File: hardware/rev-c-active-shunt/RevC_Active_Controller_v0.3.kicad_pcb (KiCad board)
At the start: 2 copper layers, 60 x 40 mm, 29 parts, among them J1 TEST_A / GND, J2 +12 GND -12, U1 OPA551PA

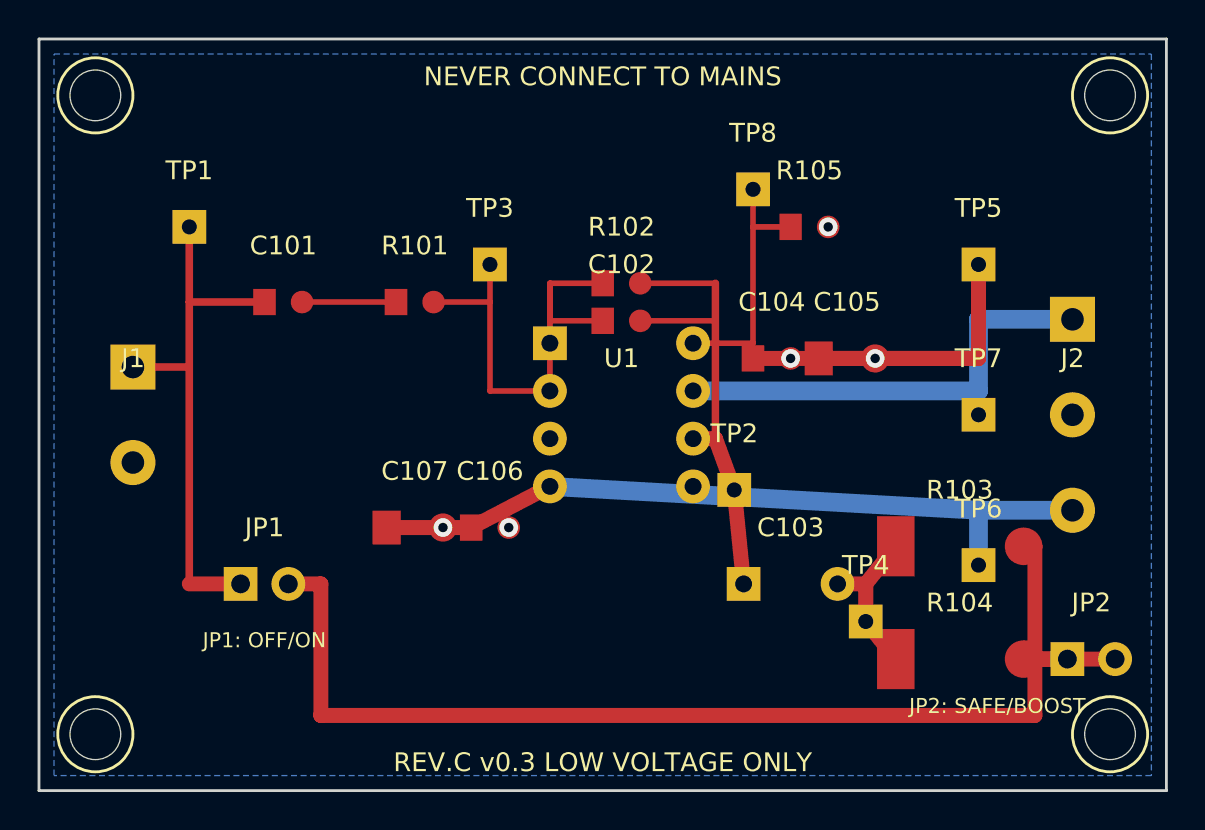
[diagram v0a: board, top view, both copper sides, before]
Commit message: Rev.C v0.3.1: fix pin mapping, parity, libraries, and PCB routing
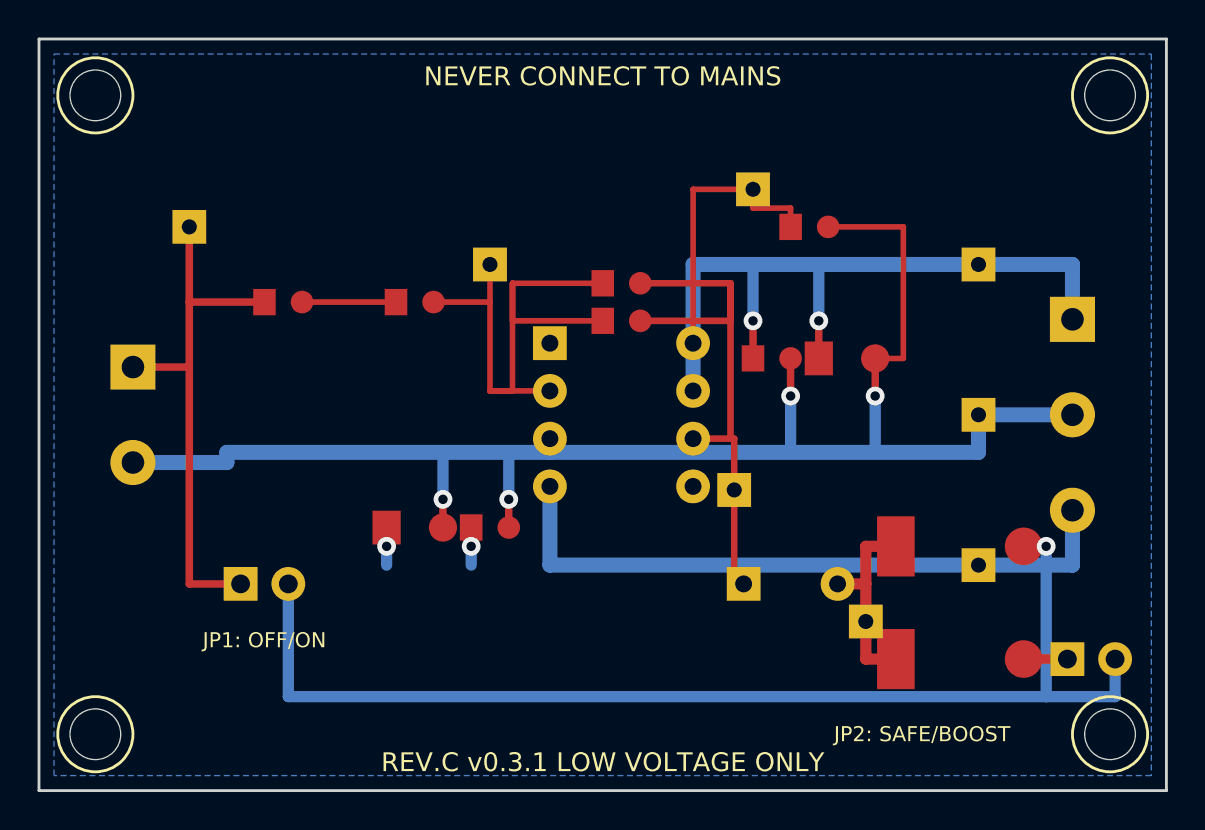
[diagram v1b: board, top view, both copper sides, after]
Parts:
- C103: footprint Capacitor_THT:C_Rect_L7.2mm_W4.5mm_P5.00mm -> RevC:C_FILM_P5
- H1, H2, H3, H4: renamed from ?; value (none) -> MountingHole
- J2: value +12 GND -12 -> +12/GND/-12
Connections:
- net +12V renamed /+12V
- net -12V renamed /-12V
- net ACTIVE_SW renamed /ACTIVE_SW
- net BOOST_SW renamed /BOOST_SW
- net FLAG renamed /FLAG
- net GND renamed /GND
- net INJ_NODE renamed /INJ_NODE
- net NINV renamed /NINV
- net OUT renamed /OUT
- net SENSE_CAP renamed /SENSE_CAP
- net TEST_A renamed /TEST_A
- U1 pad 1: NC1 -> (no net)
- U1 pad 5: NC5 -> (no net)
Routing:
- net /GND: track 0.00 -> 83.8 mm, vias 5 -> 4
- net /+12V: track 49.5 -> 39.8 mm, vias 0 -> 2
- net /NINV: track 26.3 -> 31.5 mm
- net /OUT: track 27.4 -> 30.3 mm
- net /INJ_NODE: track 8.62 -> 10.7 mm
- net /FLAG: track 13.4 -> 15.4 mm
- net /-12V: track 40.0 -> 38.9 mm, vias 0 -> 2
- net /ACTIVE_SW: track 60.6 -> 61.2 mm, vias 0 -> 1
- added copper zone on B.Cu, net GND
- removed copper zone on B.Cu, net /GND
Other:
- board text added: "REV.C v0.3.1 LOW VOLTAGE ONLY"
- board text removed: "REV.C v0.3 LOW VOLTAGE ONLY"
